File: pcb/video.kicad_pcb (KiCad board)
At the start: 2 copper layers, 159.9 x 99.9 mm, 4 parts

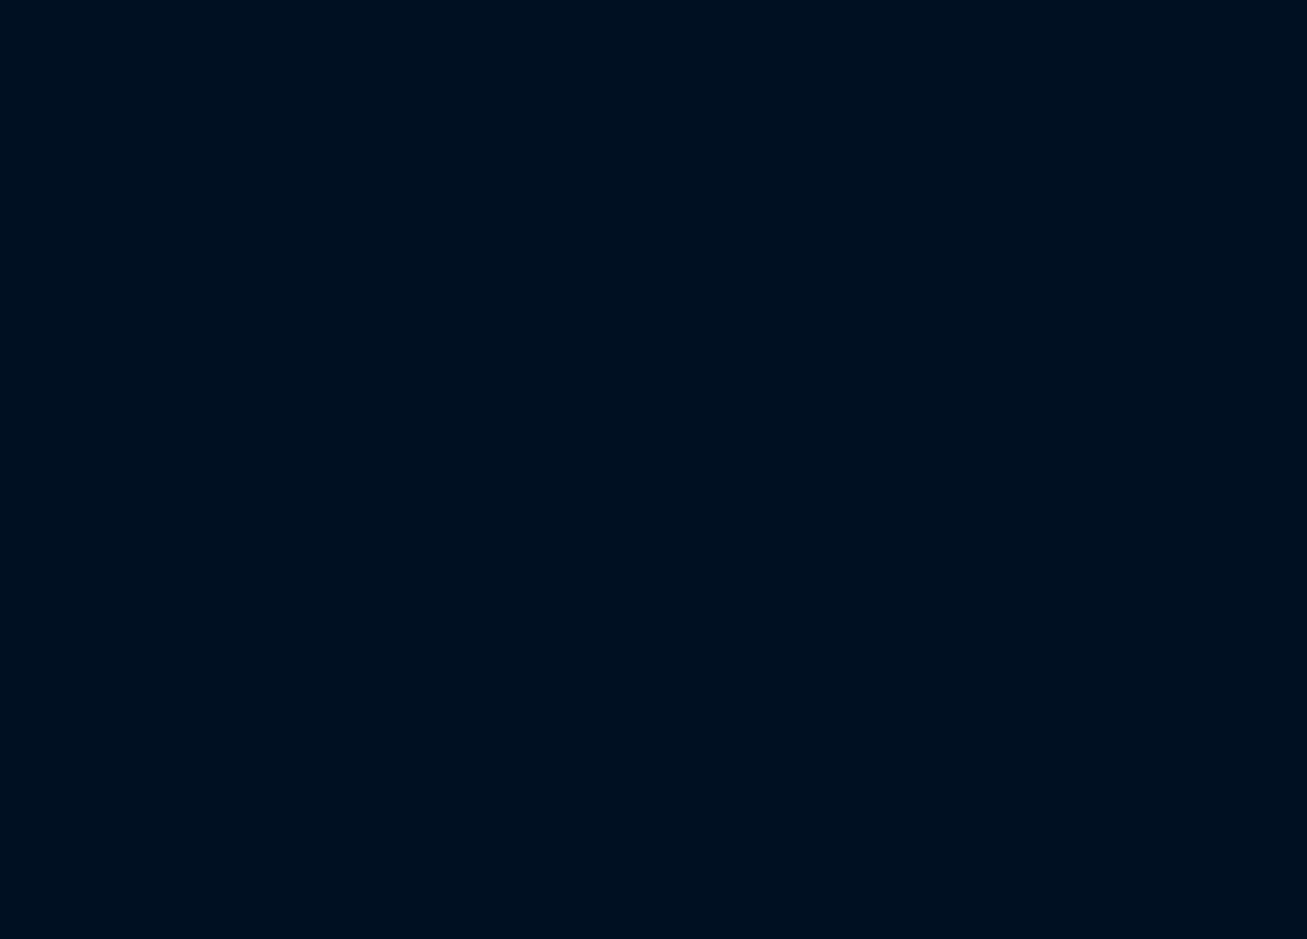
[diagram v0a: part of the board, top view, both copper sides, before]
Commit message: choose components and add footprints
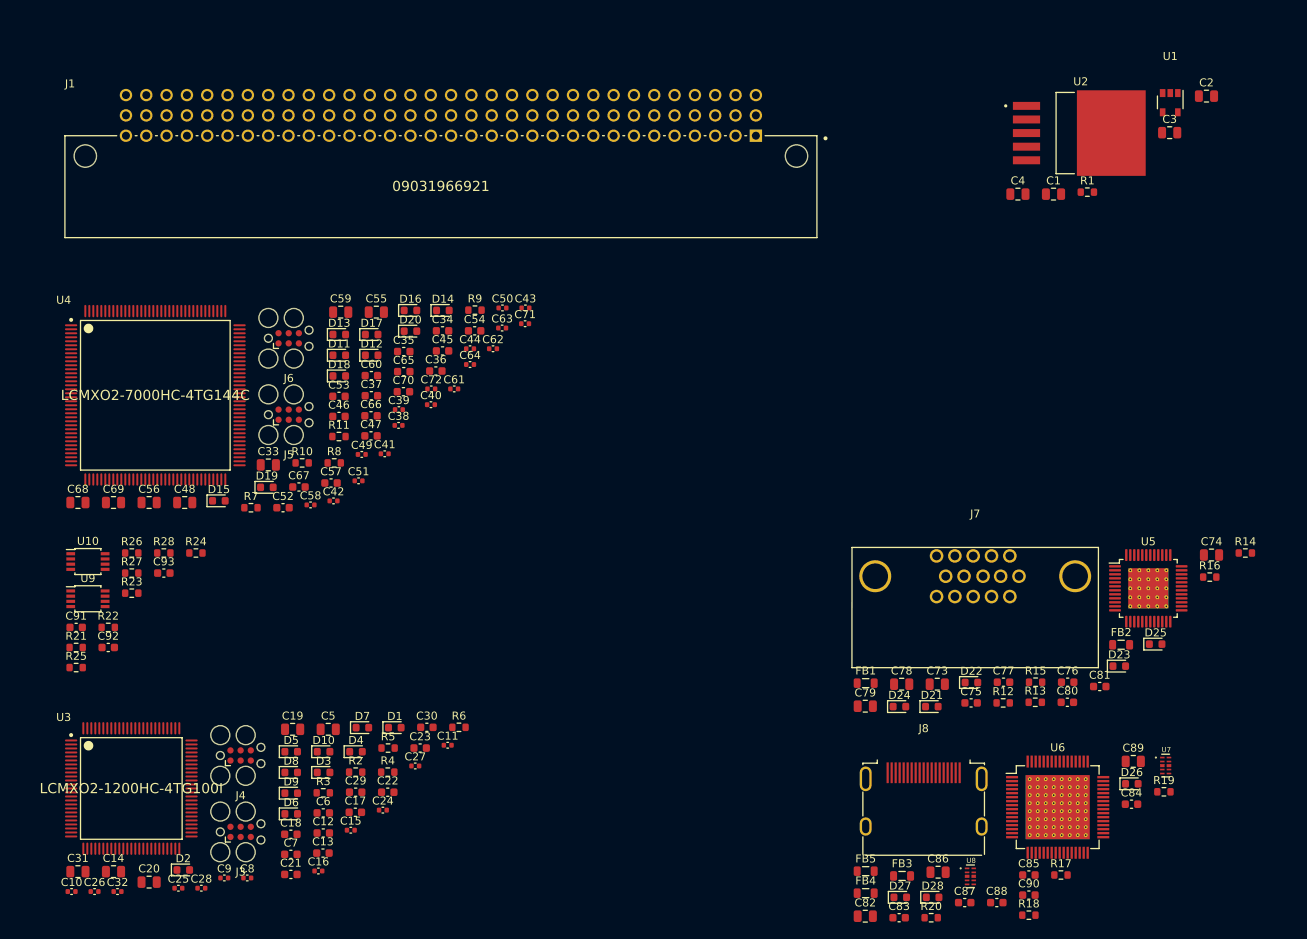
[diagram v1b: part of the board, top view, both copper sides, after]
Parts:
- added C1: 10u, Capacitor_SMD:C_0805_2012Metric, F.Cu at (-30.6, 71.9)
- added C10: 10n, Capacitor_SMD:C_0402_1005Metric, F.Cu at (-153.4, 159.1)
- added C11: 10n, Capacitor_SMD:C_0402_1005Metric, F.Cu at (-106.3, 140.8)
- added C12: 100n, Capacitor_SMD:C_0603_1608Metric, F.Cu at (-121.9, 151.8)
- added C13: 100n, Capacitor_SMD:C_0603_1608Metric, F.Cu at (-121.9, 154.3)
- added C14: 1u, Capacitor_SMD:C_0805_2012Metric, F.Cu at (-148.1, 156.6)
- added C15: 10n, Capacitor_SMD:C_0402_1005Metric, F.Cu at (-118.5, 151.4)
- added C16: 10n, Capacitor_SMD:C_0402_1005Metric, F.Cu at (-122.5, 156.5)
- added C17: 100n, Capacitor_SMD:C_0603_1608Metric, F.Cu at (-117.9, 149.2)
- added C18: 100n, Capacitor_SMD:C_0603_1608Metric, F.Cu at (-126.0, 151.9)
- added C19: 1u, Capacitor_SMD:C_0805_2012Metric, F.Cu at (-125.7, 138.8)
- added C2: 10u, Capacitor_SMD:C_0805_2012Metric, F.Cu at (-11.5, 59.7)
- added C20: 1u, Capacitor_SMD:C_0805_2012Metric, F.Cu at (-143.7, 157.9)
- added C21: 100n, Capacitor_SMD:C_0603_1608Metric, F.Cu at (-126.0, 157.0)
- added C22: 100n, Capacitor_SMD:C_0603_1608Metric, F.Cu at (-113.8, 146.7)
- added C23: 100n, Capacitor_SMD:C_0603_1608Metric, F.Cu at (-109.8, 141.2)
- added C24: 10n, Capacitor_SMD:C_0402_1005Metric, F.Cu at (-114.5, 148.9)
- added C25: 10n, Capacitor_SMD:C_0402_1005Metric, F.Cu at (-140.0, 158.7)
- added C26: 10n, Capacitor_SMD:C_0402_1005Metric, F.Cu at (-150.5, 159.1)
- added C27: 10n, Capacitor_SMD:C_0402_1005Metric, F.Cu at (-110.4, 143.4)
- added C28: 10n, Capacitor_SMD:C_0402_1005Metric, F.Cu at (-137.1, 158.7)
- added C29: 100n, Capacitor_SMD:C_0603_1608Metric, F.Cu at (-117.8, 146.7)
- added C3: 10u, Capacitor_SMD:C_0805_2012Metric, F.Cu at (-16.1, 64.2)
- added C30: 100n, Capacitor_SMD:C_0603_1608Metric, F.Cu at (-109.0, 138.6)
- added C31: 1u, Capacitor_SMD:C_0805_2012Metric, F.Cu at (-152.6, 156.6)
- added C32: 100p, Capacitor_SMD:C_0402_1005Metric, F.Cu at (-147.6, 159.1)
- added C33: 1u, Capacitor_SMD:C_0805_2012Metric, F.Cu at (-128.8, 105.8)
- added C34: 100n, Capacitor_SMD:C_0603_1608Metric, F.Cu at (-107.0, 89.0)
- added C35: 100n, Capacitor_SMD:C_0603_1608Metric, F.Cu at (-111.8, 91.6)
- added C36: 100n, Capacitor_SMD:C_0603_1608Metric, F.Cu at (-107.8, 94.0)
- added C37: 100n, Capacitor_SMD:C_0603_1608Metric, F.Cu at (-115.9, 97.1)
- added C38: 10n, Capacitor_SMD:C_0402_1005Metric, F.Cu at (-112.5, 100.8)
- added C39: 10n, Capacitor_SMD:C_0402_1005Metric, F.Cu at (-112.5, 98.9)
- added C4: 10u, Capacitor_SMD:C_0805_2012Metric, F.Cu at (-35.1, 71.9)
- added C40: 10n, Capacitor_SMD:C_0402_1005Metric, F.Cu at (-108.4, 98.2)
- added C41: 10n, Capacitor_SMD:C_0402_1005Metric, F.Cu at (-114.2, 104.4)
- added C42: 10n, Capacitor_SMD:C_0402_1005Metric, F.Cu at (-120.6, 110.3)
- added C43: 10n, Capacitor_SMD:C_0402_1005Metric, F.Cu at (-96.6, 86.2)
- added C44: 10n, Capacitor_SMD:C_0402_1005Metric, F.Cu at (-103.5, 91.3)
- added C45: 100n, Capacitor_SMD:C_0603_1608Metric, F.Cu at (-107.0, 91.5)
- added C46: 100n, Capacitor_SMD:C_0603_1608Metric, F.Cu at (-119.9, 99.7)
- added C47: 100n, Capacitor_SMD:C_0603_1608Metric, F.Cu at (-115.9, 102.2)
- added C48: 1u, Capacitor_SMD:C_0805_2012Metric, F.Cu at (-139.2, 110.5)
- added C49: 10n, Capacitor_SMD:C_0402_1005Metric, F.Cu at (-117.1, 104.5)
- added C5: 1u, Capacitor_SMD:C_0805_2012Metric, F.Cu at (-121.3, 138.8)
- added C50: 10n, Capacitor_SMD:C_0402_1005Metric, F.Cu at (-99.5, 86.2)
- added C51: 10n, Capacitor_SMD:C_0402_1005Metric, F.Cu at (-117.5, 107.8)
- added C52: 100n, Capacitor_SMD:C_0603_1608Metric, F.Cu at (-126.9, 111.1)
- added C53: 100n, Capacitor_SMD:C_0603_1608Metric, F.Cu at (-119.9, 97.2)
- added C54: 100n, Capacitor_SMD:C_0603_1608Metric, F.Cu at (-103.0, 89.0)
- added C55: 1u, Capacitor_SMD:C_0805_2012Metric, F.Cu at (-115.3, 86.7)
- added C56: 1u, Capacitor_SMD:C_0805_2012Metric, F.Cu at (-143.7, 110.5)
- added C57: 100n, Capacitor_SMD:C_0603_1608Metric, F.Cu at (-120.9, 108.0)
- added C58: 1n, Capacitor_SMD:C_0402_1005Metric, F.Cu at (-123.5, 110.8)
- added C59: 1u, Capacitor_SMD:C_0805_2012Metric, F.Cu at (-119.7, 86.7)
- added C6: 100n, Capacitor_SMD:C_0603_1608Metric, F.Cu at (-121.9, 149.3)
- added C60: 100n, Capacitor_SMD:C_0603_1608Metric, F.Cu at (-115.9, 94.6)
- added C61: 1n, Capacitor_SMD:C_0402_1005Metric, F.Cu at (-105.5, 96.3)
- added C62: 10n, Capacitor_SMD:C_0402_1005Metric, F.Cu at (-100.7, 91.3)
- added C63: 10n, Capacitor_SMD:C_0402_1005Metric, F.Cu at (-99.5, 88.7)
- added C64: 10n, Capacitor_SMD:C_0402_1005Metric, F.Cu at (-103.5, 93.2)
- added C65: 100n, Capacitor_SMD:C_0603_1608Metric, F.Cu at (-111.8, 94.1)
- added C66: 100n, Capacitor_SMD:C_0603_1608Metric, F.Cu at (-115.9, 99.6)
- added C67: 100n, Capacitor_SMD:C_0603_1608Metric, F.Cu at (-124.9, 108.5)
- added C68: 1u, Capacitor_SMD:C_0805_2012Metric, F.Cu at (-152.6, 110.5)
- added C69: 1u, Capacitor_SMD:C_0805_2012Metric, F.Cu at (-148.1, 110.5)
- added C7: 100n, Capacitor_SMD:C_0603_1608Metric, F.Cu at (-126.0, 154.5)
- added C70: 100n, Capacitor_SMD:C_0603_1608Metric, F.Cu at (-111.9, 96.6)
- added C71: 1n, Capacitor_SMD:C_0402_1005Metric, F.Cu at (-96.7, 88.1)
- added C72: 100p, Capacitor_SMD:C_0402_1005Metric, F.Cu at (-108.4, 96.3)
- added C73: 10u, Capacitor_SMD:C_0805_2012Metric, F.Cu at (-45.1, 133.2)
- added C74: 10u, Capacitor_SMD:C_0805_2012Metric, F.Cu at (-10.9, 117.0)
- added C75: 100n, Capacitor_SMD:C_0603_1608Metric, F.Cu at (-40.9, 135.5)
- added C76: 100n, Capacitor_SMD:C_0603_1608Metric, F.Cu at (-28.9, 132.9)
- added C77: 100n, Capacitor_SMD:C_0603_1608Metric, F.Cu at (-36.9, 132.9)
- added C78: 10u, Capacitor_SMD:C_0805_2012Metric, F.Cu at (-49.6, 133.2)
- added C79: 10u, Capacitor_SMD:C_0805_2012Metric, F.Cu at (-54.1, 135.9)
- added C8: 10n, Capacitor_SMD:C_0402_1005Metric, F.Cu at (-131.4, 157.4)
- added C80: 100n, Capacitor_SMD:C_0603_1608Metric, F.Cu at (-28.9, 135.4)
- added C81: 100n, Capacitor_SMD:C_0603_1608Metric, F.Cu at (-24.8, 133.5)
- added C82: 10u, Capacitor_SMD:C_0805_2012Metric, F.Cu at (-54.1, 162.2)
- added C83: 100n, Capacitor_SMD:C_0603_1608Metric, F.Cu at (-49.9, 162.4)
- added C84: 100n, Capacitor_SMD:C_0603_1608Metric, F.Cu at (-20.9, 148.2)
- added C85: 100n, Capacitor_SMD:C_0603_1608Metric, F.Cu at (-33.7, 157.0)
- added C86: 10u, Capacitor_SMD:C_0805_2012Metric, F.Cu at (-45.0, 156.7)
- added C87: 100n, Capacitor_SMD:C_0603_1608Metric, F.Cu at (-41.7, 160.5)
- added C88: 100n, Capacitor_SMD:C_0603_1608Metric, F.Cu at (-37.7, 160.5)
- added C89: 10u, Capacitor_SMD:C_0805_2012Metric, F.Cu at (-20.6, 142.8)
- added C9: 10n, Capacitor_SMD:C_0402_1005Metric, F.Cu at (-134.3, 157.4)
- added C90: 100n, Capacitor_SMD:C_0603_1608Metric, F.Cu at (-33.7, 159.6)
- added C91: 100n, Capacitor_SMD:C_0603_1608Metric, F.Cu at (-152.8, 126.1)
- added C92: 100n, Capacitor_SMD:C_0603_1608Metric, F.Cu at (-148.8, 128.6)
- added C93: 100n, Capacitor_SMD:C_0603_1608Metric, F.Cu at (-141.8, 119.3)
- added D1: D_TVS, Diode_SMD:D_0603_1608Metric, F.Cu at (-113.0, 138.6)
- added D10: D_TVS, Diode_SMD:D_0603_1608Metric, F.Cu at (-121.9, 141.6)
- added D11: D_TVS, Diode_SMD:D_0603_1608Metric, F.Cu at (-119.9, 92.1)
- added D12: D_TVS, Diode_SMD:D_0603_1608Metric, F.Cu at (-115.8, 92.1)
- added D13: D_TVS, Diode_SMD:D_0603_1608Metric, F.Cu at (-119.9, 89.5)
- added D14: D_TVS, Diode_SMD:D_0603_1608Metric, F.Cu at (-107.0, 86.5)
- added D15: D_TVS, Diode_SMD:D_0603_1608Metric, F.Cu at (-134.9, 110.3)
- added D16: D_TVS, Diode_SMD:D_0603_1608Metric, F.Cu at (-111.0, 86.5)
- added D17: D_TVS, Diode_SMD:D_0603_1608Metric, F.Cu at (-115.8, 89.5)
- added D18: D_TVS, Diode_SMD:D_0603_1608Metric, F.Cu at (-119.9, 94.7)
- added D19: D_TVS, Diode_SMD:D_0603_1608Metric, F.Cu at (-128.9, 108.6)
- added D2: D_TVS, Diode_SMD:D_0603_1608Metric, F.Cu at (-139.4, 156.4)
- added D20: D_TVS, Diode_SMD:D_0603_1608Metric, F.Cu at (-111.0, 89.1)
- added D21: D_TVS, Diode_SMD:D_0603_1608Metric, F.Cu at (-45.8, 136.0)
- added D22: D_TVS, Diode_SMD:D_0603_1608Metric, F.Cu at (-40.9, 133.0)
- added D23: D_TVS, Diode_SMD:D_0603_1608Metric, F.Cu at (-22.4, 130.9)
- added D24: D_TVS, Diode_SMD:D_0603_1608Metric, F.Cu at (-49.9, 136.0)
- added D25: D_TVS, Diode_SMD:D_0603_1608Metric, F.Cu at (-17.9, 128.2)
- added D26: D_TVS, Diode_SMD:D_0603_1608Metric, F.Cu at (-20.8, 145.6)
- added D27: D_TVS, Diode_SMD:D_0603_1608Metric, F.Cu at (-49.8, 159.8)
- added D28: D_TVS, Diode_SMD:D_0603_1608Metric, F.Cu at (-45.7, 159.8)
- added D3: D_TVS, Diode_SMD:D_0603_1608Metric, F.Cu at (-121.9, 144.2)
- added D4: D_TVS, Diode_SMD:D_0603_1608Metric, F.Cu at (-117.8, 141.6)
- added D5: D_TVS, Diode_SMD:D_0603_1608Metric, F.Cu at (-125.9, 141.6)
- added D6: D_TVS, Diode_SMD:D_0603_1608Metric, F.Cu at (-125.9, 149.4)
- added D7: D_TVS, Diode_SMD:D_0603_1608Metric, F.Cu at (-117.0, 138.6)
- added D8: D_TVS, Diode_SMD:D_0603_1608Metric, F.Cu at (-125.9, 144.2)
- added D9: D_TVS, Diode_SMD:D_0603_1608Metric, F.Cu at (-125.9, 146.8)
- added FB1: FerriteBead_Small, Inductor_SMD:L_0805_2012Metric, F.Cu at (-54.1, 133.1)
- added FB2: FerriteBead_Small, Inductor_SMD:L_0805_2012Metric, F.Cu at (-22.2, 128.3)
- added FB3: FerriteBead_Small, Inductor_SMD:L_0805_2012Metric, F.Cu at (-49.5, 157.2)
- added FB4: FerriteBead_Small, Inductor_SMD:L_0805_2012Metric, F.Cu at (-54.1, 159.3)
- added FB5: FerriteBead_Small, Inductor_SMD:L_0805_2012Metric, F.Cu at (-54.1, 156.6)
- added J1: 09031966921, 09031966821:Harting-09031966921-0-0-0, F.Cu at (-107.2, 70.9)
- added J3: Conn_01x06, Connector:Tag-Connect_TC2030-IDC-FP_2x03_P1.27mm_Vertical, F.Cu at (-132.2, 151.7)
- added J4: Conn_01x06, Connector:Tag-Connect_TC2030-IDC-FP_2x03_P1.27mm_Vertical, F.Cu at (-132.2, 142.1)
- added J5: Conn_01x06, Connector:Tag-Connect_TC2030-IDC-FP_2x03_P1.27mm_Vertical, F.Cu at (-126.2, 99.5)
- added J6: Conn_01x06, Connector:Tag-Connect_TC2030-IDC-FP_2x03_P1.27mm_Vertical, F.Cu at (-126.2, 90.0)
- added J7: DB15_Female_HighDensity, L77HDE15SD1CH4FVGA:L77HDE15SD1CH4FVGA, F.Cu at (-40.4, 119.7)
- added J8: HDMI_A, RAHHD19TR:RAAHD19TR, F.Cu at (-46.9, 144.3)
- added R1: 10k, Resistor_SMD:R_0603_1608Metric, F.Cu at (-26.4, 71.7)
- added R10: 10k, Resistor_SMD:R_0603_1608Metric, F.Cu at (-124.5, 105.5)
- added R11: 10k, Resistor_SMD:R_0603_1608Metric, F.Cu at (-119.9, 102.2)
- added R12: 75, Resistor_SMD:R_0603_1608Metric, F.Cu at (-36.9, 135.5)
- added R13: 75, Resistor_SMD:R_0603_1608Metric, F.Cu at (-32.9, 135.4)
- added R14: 75, Resistor_SMD:R_0603_1608Metric, F.Cu at (-6.64, 116.8)
- added R15: 2.2k, Resistor_SMD:R_0603_1608Metric, F.Cu at (-32.9, 132.9)
- added R16: 3.8k, Resistor_SMD:R_0603_1608Metric, F.Cu at (-11.1, 119.8)
- added R17: 10k, Resistor_SMD:R_0603_1608Metric, F.Cu at (-29.7, 157.0)
- added R18: 510 @ 1%, Resistor_SMD:R_0603_1608Metric, F.Cu at (-33.7, 162.1)
- added R19: 1k, Resistor_SMD:R_0603_1608Metric, F.Cu at (-16.8, 146.6)
- added R2: 10k, Resistor_SMD:R_0603_1608Metric, F.Cu at (-117.8, 144.2)
- added R20: 10k, Resistor_SMD:R_0603_1608Metric, F.Cu at (-45.9, 162.4)
- added R21: 10k, Resistor_SMD:R_0603_1608Metric, F.Cu at (-152.8, 128.6)
- added R22: 10k, Resistor_SMD:R_0603_1608Metric, F.Cu at (-148.8, 126.1)
- added R23: 10k, Resistor_SMD:R_0603_1608Metric, F.Cu at (-145.8, 121.8)
- added R24: 10k, Resistor_SMD:R_0603_1608Metric, F.Cu at (-137.8, 116.8)
- added R25: 10k, Resistor_SMD:R_0603_1608Metric, F.Cu at (-152.8, 131.1)
- added R26: 10k, Resistor_SMD:R_0603_1608Metric, F.Cu at (-145.8, 116.8)
- added R27: 10k, Resistor_SMD:R_0603_1608Metric, F.Cu at (-145.8, 119.3)
- added R28: 10k, Resistor_SMD:R_0603_1608Metric, F.Cu at (-141.8, 116.8)
- added R3: 10k, Resistor_SMD:R_0603_1608Metric, F.Cu at (-121.9, 146.8)
- added R4: 10k, Resistor_SMD:R_0603_1608Metric, F.Cu at (-113.8, 144.2)
- added R5: 10k, Resistor_SMD:R_0603_1608Metric, F.Cu at (-113.8, 141.2)
- added R6: 10k, Resistor_SMD:R_0603_1608Metric, F.Cu at (-104.9, 138.6)
- added R7: 10k, Resistor_SMD:R_0603_1608Metric, F.Cu at (-130.9, 111.1)
- added R8: 10k, Resistor_SMD:R_0603_1608Metric, F.Cu at (-120.5, 105.5)
- added R9: 10k, Resistor_SMD:R_0603_1608Metric, F.Cu at (-102.9, 86.4)
- added U1: NCP115, NCP115ASN180T2G:NCP115ASN180T2G, F.Cu at (-16.0, 59.3)
- added U10: NCA9306DPH, Package_SO:TSSOP-8_3x3mm_P0.65mm, F.Cu at (-151.3, 117.9)
- added U2: LP3853ESX-3.3/NOPB, LP3853ESX-3_3:LP3853ESX-3_3, F.Cu at (-23.4, 64.3)
- added U3: LCMXO2-1200HC-4TG100I, LCMXO2-1200HC-4TG100I:Lattice_Semiconductor-LCMXO2-1200HC-4TG100I-Level_C, F.Cu at (-145.9, 146.2)
- added U4: LCMXO2-7000HC-4TG144C, LCMXO2-7000HC-4TG144C:Lattice_Semiconductor-LCMXO2-7000HC-4TG144C-Level_C, F.Cu at (-142.9, 97.1)
- added U5: THS8136, Package_QFP:TQFP-48-1EP_7x7mm_P0.5mm_EP5x5mm_ThermalVias, F.Cu at (-18.8, 121.2)
- added U6: TFP410PAP, Package_QFP:HTQFP-64-1EP_10x10mm_P0.5mm_EP8x8mm_Mask4.4x4.4mm_ThermalVias, F.Cu at (-30.1, 148.6)
- added U7: ESD224DQA, ESD224DQA:IC_TPD4EUSB30DQAR, F.Cu at (-16.6, 143.4)
- added U8: ESD224DQA, ESD224DQA:IC_TPD4EUSB30DQAR, F.Cu at (-41.0, 157.2)
- added U9: PCA9540BDP, Package_SO:TSSOP-8_3x3mm_P0.65mm, F.Cu at (-151.3, 122.5)

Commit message: add video controller oscillator
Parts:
- added C94: 10n, Capacitor_SMD:C_0402_1005Metric, F.Cu at (91.0, 159.9)
- added X1: ASV-xxxMHz, Oscillator:Oscillator_SMD_Abracon_ASV-4Pin_7.0x5.1mm, F.Cu at (85.2, 162.8)
- J3, J4, J5, J6: footprint Connector:Tag-Connect_TC2030-IDC-FP_2x03_P1.27mm_Vertical -> Connector:Tag-Connect_TC2030-IDC-NL_2x03_P1.27mm_Vertical
- moved J4 340.4 mm to (207.9, 156.9), turned to -90 degrees
- moved U3 330.9 mm to (181.0, 95.0), turned to -90 degrees
- moved J3 330.6 mm to (198.3, 156.9), turned to -90 degrees
- moved C9 326.9 mm to (192.6, 154.9), turned to -90 degrees
- moved J1 324.1 mm to (216.1, 94.9), turned to 90 degrees
- moved C8 324.0 mm to (192.6, 157.7), turned to -90 degrees
- moved C31 322.2 mm to (169.7, 158.5), turned to -90 degrees
- moved C10 320.5 mm to (167.2, 157.7), turned to -90 degrees
- moved C14 317.8 mm to (169.7, 162.9), turned to -90 degrees
- moved C26 317.7 mm to (167.2, 160.6), turned to -90 degrees
- moved C19 315.2 mm to (189.2, 152.9), turned to -90 degrees
- moved C32 314.8 mm to (167.2, 163.4), turned to -90 degrees
- moved D5 312.5 mm to (186.4, 152.8), turned to -90 degrees
- moved C20 312.2 mm to (168.3, 167.4), turned to -90 degrees
- moved C5 311.0 mm to (189.2, 157.4), turned to -90 degrees
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
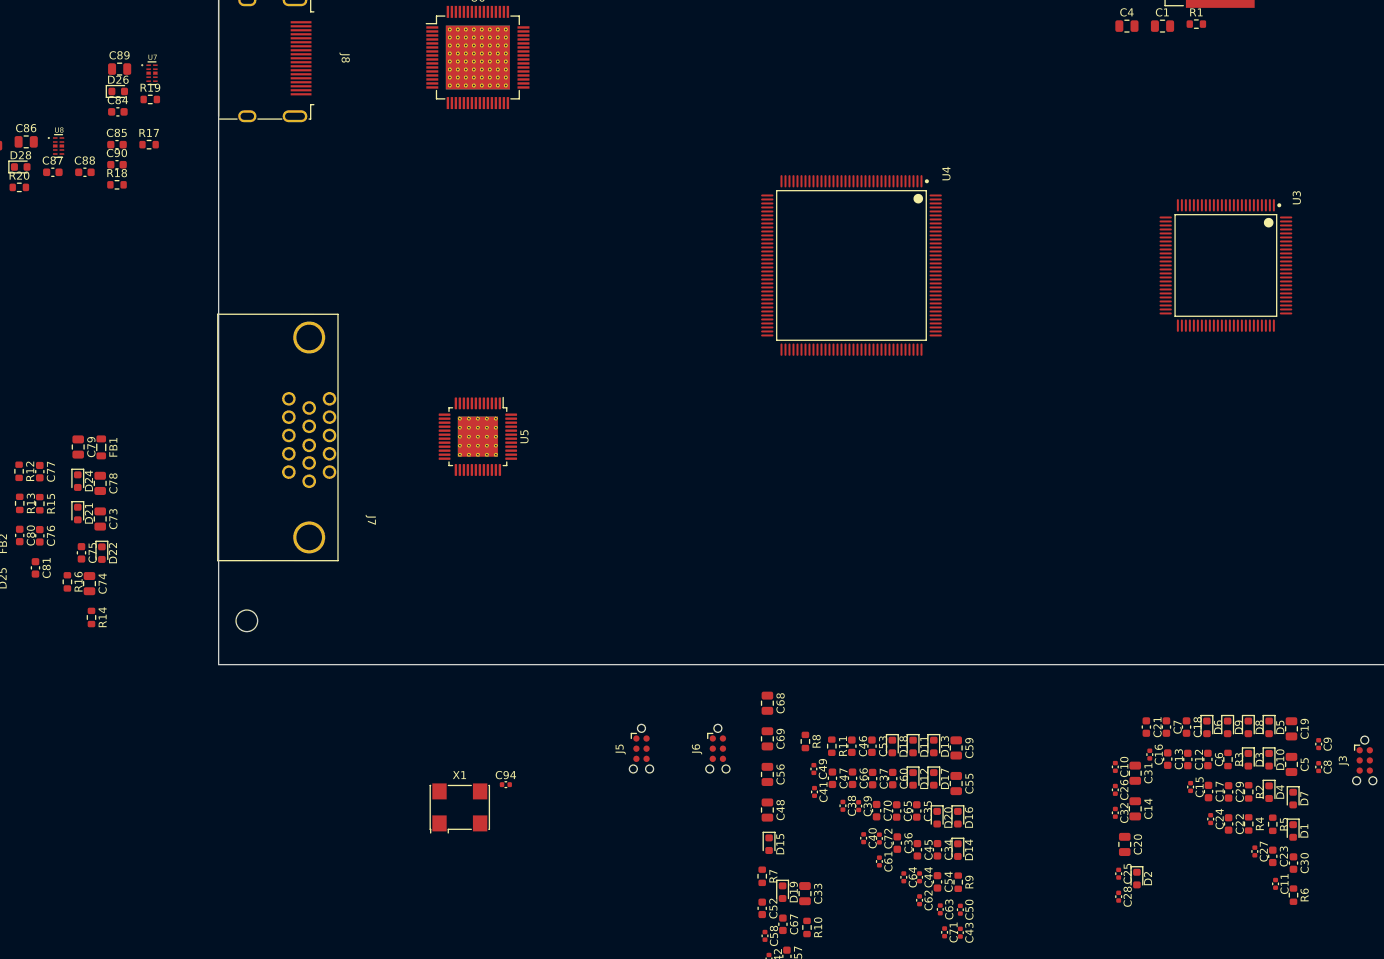
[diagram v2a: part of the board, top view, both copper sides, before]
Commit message: add decoupling caps on bus controller
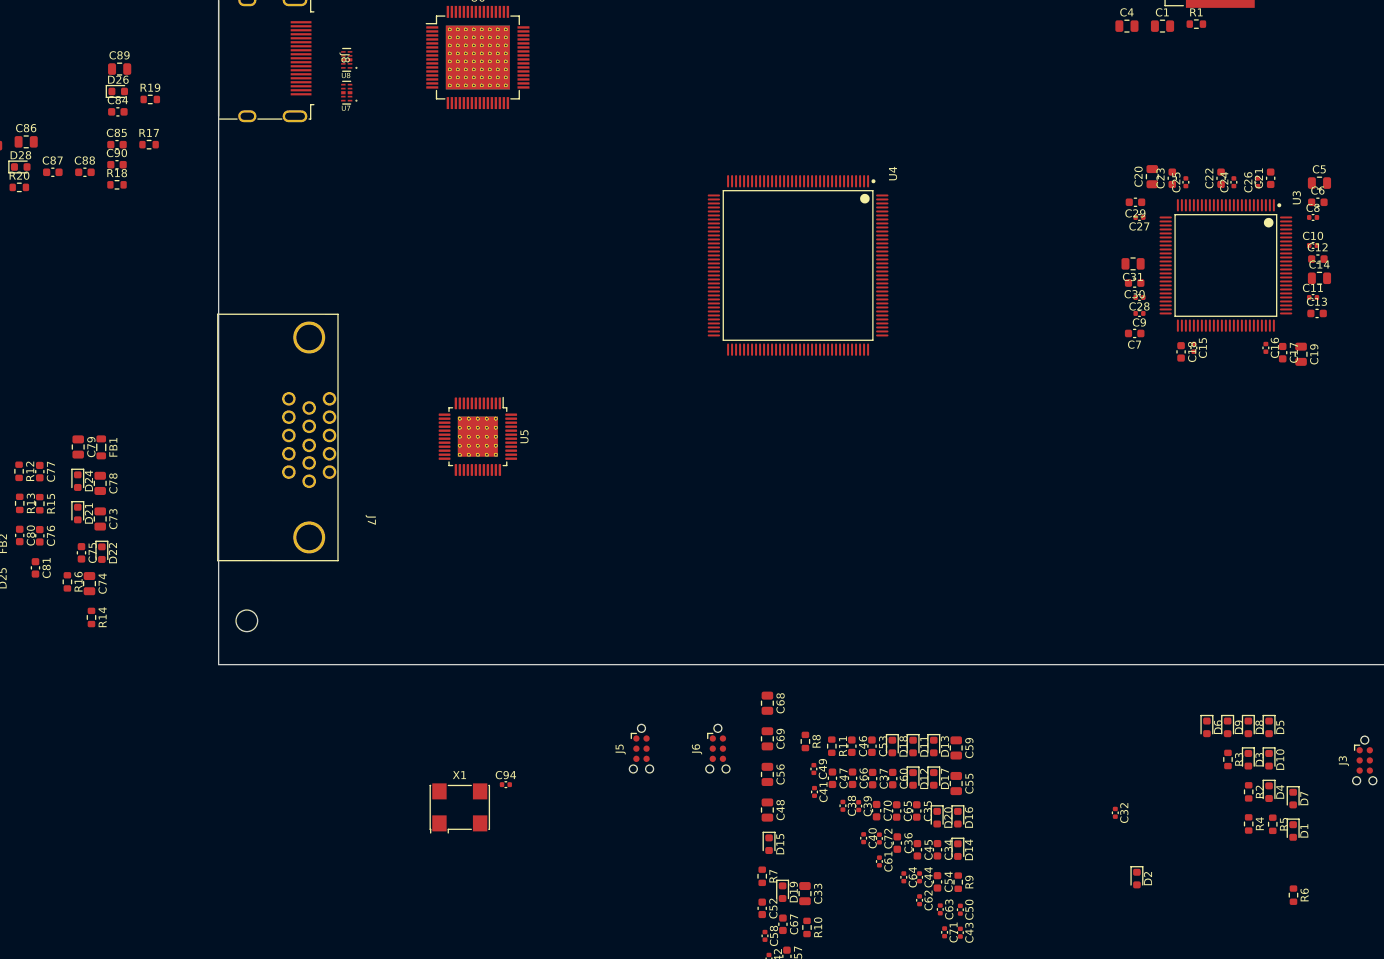
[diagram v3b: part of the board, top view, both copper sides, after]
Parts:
- moved C25 86.8 mm to (176.0, 84.6), turned to 90 degrees
- moved C23 85.7 mm to (174.3, 84.1), turned to 90 degrees
- moved C20 83.5 mm to (171.8, 83.9), turned to 90 degrees
- moved C22 80.7 mm to (180.4, 84.1), turned to 90 degrees
- moved C27 80.6 mm to (170.2, 89.0), turned to 180 degrees
- moved C24 79.7 mm to (182.0, 84.6), turned to 90 degrees
- moved C26 78.0 mm to (185.0, 84.6), turned to 90 degrees
- moved C30 75.2 mm to (169.6, 97.2), turned to 180 degrees
- moved C28 74.9 mm to (170.2, 99.0), turned to 180 degrees
- moved C29 74.6 mm to (169.7, 87.1), turned to 180 degrees
- moved C11 73.4 mm to (191.9, 99.0), turned to 0 degrees
- moved C5 72.8 mm to (192.7, 84.7), turned to 0 degrees
- moved C6 71.0 mm to (192.5, 87.1), turned to 0 degrees
- moved C21 70.3 mm to (186.6, 84.1), turned to 90 degrees
- moved C14 70.2 mm to (192.7, 96.6), turned to 0 degrees
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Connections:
- U3 pad 93: unconnected-(U3E-VCCIO0) -> +3V3
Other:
- copper layers 2 -> 4
